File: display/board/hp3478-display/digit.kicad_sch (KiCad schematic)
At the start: 18 parts

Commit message: Reorganize schematic.
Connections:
- net A16: no longer D218.2 (A)
- net K: no longer D217.1 (K)
- new net: D217.1 (K), D218.2 (A)
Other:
- moved on the sheet: D201, D202, D203, D204, D205, D206, D207, D208, D209, D210, D211, D212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

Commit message: Add digit outlines and place LEDs.
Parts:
- D201, D202, D203, D204, D205, D206, D207, D208, D209, D210, D211, D212, D213, D214, D215, D216, D217, D218: footprint LED_SMD:LED_0402_1005Metric -> 0Local:LED_0402_1005Metric
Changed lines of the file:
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@@
       (effects (font (size 1.27 1.27)) (justify right))
     )
-    (property "Footprint" "LED_SMD:LED_0402_1005Metric" (id 2) (at 74.93 88.9 0)
+    (property "Footprint" "0Local:LED_0402_1005Metric" (id 2) (at 74.93 88.9 0)
       (effects (font (size 1.27 1.27)) hide)
     )
@@
       (effects (font (size 1.27 1.27)) (justify right))
     )
-    (property "Footprint" "LED_SMD:LED_0402_1005Metric" (id 2) (at 87.63 142.24 0)
+    (property "Footprint" "0Local:LED_0402_1005Metric" (id 2) (at 87.63 142.24 0)
       (effects (font (size 1.27 1.27)) hide)
     )
@@
       (effects (font (size 1.27 1.27)) (justify right))
     )
-    (property "Footprint" "LED_SMD:LED_0402_1005Metric" (id 2) (at 74.93 68.58 0)
+    (property "Footprint" "0Local:LED_0402_1005Metric" (id 2) (at 74.93 68.58 0)
       (effects (font (size 1.27 1.27)) hide)
     )
@@
       (effects (font (size 1.27 1.27)) (justify right))
     )
-    (property "Footprint" "LED_SMD:LED_0402_1005Metric" (id 2) (at 74.93 93.98 0)
+    (property "Footprint" "0Local:LED_0402_1005Metric" (id 2) (at 74.93 93.98 0)
       (effects (font (size 1.27 1.27)) hide)
     )
@@
       (effects (font (size 1.27 1.27)) (justify right))
     )
-    (property "Footprint" "LED_SMD:LED_0402_1005Metric" (id 2) (at 74.93 104.14 0)
+    (property "Footprint" "0Local:LED_0402_1005Metric" (id 2) (at 74.93 104.14 0)
       (effects (font (size 1.27 1.27)) hide)
     )
@@
       (effects (font (size 1.27 1.27)) (justify right))
     )
-    (property "Footprint" "LED_SMD:LED_0402_1005Metric" (id 2) (at 74.93 73.66 0)
+    (property "Footprint" "0Local:LED_0402_1005Metric" (id 2) (at 74.93 73.66 0)
       (effects (font (size 1.27 1.27)) hide)
     )
@@
       (effects (font (size 1.27 1.27)) (justify right))
     )
-    (property "Footprint" "LED_SMD:LED_0402_1005Metric" (id 2) (at 74.93 119.38 0)
+    (property "Footprint" "0Local:LED_0402_1005Metric" (id 2) (at 74.93 119.38 0)
       (effects (font (size 1.27 1.27)) hide)
     )
@@
       (effects (font (size 1.27 1.27)) (justify right))
     )
-    (property "Footprint" "LED_SMD:LED_0402_1005Metric" (id 2) (at 74.93 124.46 0)
+    (property "Footprint" "0Local:LED_0402_1005Metric" (id 2) (at 74.93 124.46 0)
       (effects (font (size 1.27 1.27)) hide)
     )
@@
       (effects (font (size 1.27 1.27)) (justify right))
     )
-    (property "Footprint" "LED_SMD:LED_0402_1005Metric" (id 2) (at 74.93 114.3 0)
+    (property "Footprint" "0Local:LED_0402_1005Metric" (id 2) (at 74.93 114.3 0)
       (effects (font (size 1.27 1.27)) hide)
     )
@@
       (effects (font (size 1.27 1.27)) (justify right))
     )
-    (property "Footprint" "LED_SMD:LED_0402_1005Metric" (id 2) (at 74.93 58.42 0)
+    (property "Footprint" "0Local:LED_0402_1005Metric" (id 2) (at 74.93 58.42 0)
       (effects (font (size 1.27 1.27)) hide)
     )
@@
       (effects (font (size 1.27 1.27)) (justify right))
     )
-    (property "Footprint" "LED_SMD:LED_0402_1005Metric" (id 2) (at 74.93 83.82 0)
+    (property "Footprint" "0Local:LED_0402_1005Metric" (id 2) (at 74.93 83.82 0)
       (effects (font (size 1.27 1.27)) hide)
     )
@@
       (effects (font (size 1.27 1.27)) (justify right))
     )
-    (property "Footprint" "LED_SMD:LED_0402_1005Metric" (id 2) (at 74.93 109.22 0)
+    (property "Footprint" "0Local:LED_0402_1005Metric" (id 2) (at 74.93 109.22 0)
       (effects (font (size 1.27 1.27)) hide)
     )
@@
       (effects (font (size 1.27 1.27)) (justify right))
     )
-    (property "Footprint" "LED_SMD:LED_0402_1005Metric" (id 2) (at 74.93 78.74 0)
+    (property "Footprint" "0Local:LED_0402_1005Metric" (id 2) (at 74.93 78.74 0)
       (effects (font (size 1.27 1.27)) hide)
     )
@@
       (effects (font (size 1.27 1.27)) (justify right))
     )
-    (property "Footprint" "LED_SMD:LED_0402_1005Metric" (id 2) (at 67.31 142.24 0)
+    (property "Footprint" "0Local:LED_0402_1005Metric" (id 2) (at 67.31 142.24 0)
       (effects (font (size 1.27 1.27)) hide)
     )
@@
       (effects (font (size 1.27 1.27)) (justify right))
     )
-    (property "Footprint" "LED_SMD:LED_0402_1005Metric" (id 2) (at 74.93 99.06 0)
+    (property "Footprint" "0Local:LED_0402_1005Metric" (id 2) (at 74.93 99.06 0)
       (effects (font (size 1.27 1.27)) hide)
     )
@@
       (effects (font (size 1.27 1.27)) (justify right))
     )
-    (property "Footprint" "LED_SMD:LED_0402_1005Metric" (id 2) (at 74.93 129.54 0)
+    (property "Footprint" "0Local:LED_0402_1005Metric" (id 2) (at 74.93 129.54 0)
       (effects (font (size 1.27 1.27)) hide)
     )
@@
       (effects (font (size 1.27 1.27)) (justify right))
     )
-    (property "Footprint" "LED_SMD:LED_0402_1005Metric" (id 2) (at 74.93 134.62 0)
+    (property "Footprint" "0Local:LED_0402_1005Metric" (id 2) (at 74.93 134.62 0)
       (effects (font (size 1.27 1.27)) hide)
     )
@@
       (effects (font (size 1.27 1.27)) (justify right))
     )
-    (property "Footprint" "LED_SMD:LED_0402_1005Metric" (id 2) (at 74.93 63.5 0)
-      (effects (font (size 1.27 1.27)) hide)
-    )
+    (property "Footprint" "0Local:LED_0402_1005Metric" (id 2) (at 74.93 63.5 0)
+      (effects (font (size 1.27 1.27)) hide)
+    )

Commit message: Remove MCU and move annunciator LEDs to their own matrix row.
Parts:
- removed D217, D218: LED, 0Local:LED_0402_1005Metric, symbol Device:LED
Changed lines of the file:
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@@
   (junction (at 101.6 124.46) (diameter 0) (color 0 0 0 0)
   )
-  (junction (at 101.6 142.24) (diameter 0) (color 0 0 0 0)
-  )
   (junction (at 101.6 88.9) (diameter 0) (color 0 0 0 0)
   )
@@
     (stroke (width 0) (type default) (color 0 0 0 0))
   )
-  (bus_entry (at 50.8 139.7) (size 2.54 2.54)
-    (stroke (width 0) (type default) (color 0 0 0 0))
-  )
   (bus_entry (at 50.8 81.28) (size 2.54 2.54)
     (stroke (width 0) (type default) (color 0 0 0 0))
@@
     (stroke (width 0) (type default) (color 0 0 0 0))
   )
-  (wire (pts (xy 53.34 142.24) (xy 63.5 142.24))
-    (stroke (width 0) (type default) (color 0 0 0 0))
-  )
   (wire (pts (xy 53.34 129.54) (xy 71.12 129.54))
     (stroke (width 0) (type default) (color 0 0 0 0))
@@
     (stroke (width 0) (type default) (color 0 0 0 0))
   )
-  (bus (pts (xy 50.8 139.7) (xy 50.8 132.08))
-    (stroke (width 0) (type default) (color 0 0 0 0))
-  )
   (bus (pts (xy 50.8 76.2) (xy 50.8 71.12))
     (stroke (width 0) (type default) (color 0 0 0 0))
@@
     (stroke (width 0) (type default) (color 0 0 0 0))
   )
-  (wire (pts (xy 91.44 157.48) (xy 101.6 157.48))
+  (wire (pts (xy 91.44 144.78) (xy 101.6 144.78))
     (stroke (width 0) (type default) (color 0 0 0 0))
   )
@@
     (stroke (width 0) (type default) (color 0 0 0 0))
   )
-  (wire (pts (xy 101.6 142.24) (xy 101.6 157.48))
-    (stroke (width 0) (type default) (color 0 0 0 0))
-  )
   (wire (pts (xy 78.74 119.38) (xy 101.6 119.38))
     (stroke (width 0) (type default) (color 0 0 0 0))
@@
     (stroke (width 0) (type default) (color 0 0 0 0))
   )
-  (wire (pts (xy 91.44 142.24) (xy 101.6 142.24))
-    (stroke (width 0) (type default) (color 0 0 0 0))
-  )
   (bus (pts (xy 50.8 96.52) (xy 50.8 91.44))
     (stroke (width 0) (type default) (color 0 0 0 0))
@@
     (stroke (width 0) (type default) (color 0 0 0 0))
   )
-  (wire (pts (xy 101.6 134.62) (xy 101.6 142.24))
+  (wire (pts (xy 101.6 134.62) (xy 101.6 144.78))
     (stroke (width 0) (type default) (color 0 0 0 0))
   )
@@
     (stroke (width 0) (type default) (color 0 0 0 0))
   )
-  (wire (pts (xy 71.12 142.24) (xy 83.82 142.24))
-    (stroke (width 0) (type default) (color 0 0 0 0))
-  )
   (wire (pts (xy 101.6 83.82) (xy 101.6 88.9))
     (stroke (width 0) (type default) (color 0 0 0 0))
@@
     (effects (font (size 1.27 1.27)) (justify left bottom))
   )
-  (label "A16" (at 55.88 142.24 0)
-    (effects (font (size 1.27 1.27)) (justify left bottom))
-  )
   (label "A11" (at 55.88 114.3 0)
     (effects (font (size 1.27 1.27)) (justify left bottom))
@@
     (effects (font (size 1.27 1.27)) (justify left bottom))
   )
-  (hierarchical_label "A[0..16]" (shape input) (at 40.64 50.8 180)
+  (hierarchical_label "A[0..15]" (shape input) (at 40.64 50.8 180)
     (effects (font (size 1.27 1.27)) (justify right))
   )
-  (hierarchical_label "K" (shape input) (at 91.44 157.48 180)
+  (hierarchical_label "K" (shape input) (at 91.44 144.78 180)
     (effects (font (size 1.27 1.27)) (justify right))
   )
@@
     )
     (property "Datasheet" "~" (id 3) (at 74.93 88.9 0)
-      (effects (font (size 1.27 1.27)) hide)
-    )
-    (pin "1")
-    (pin "2")
-  )
-  (symbol (lib_id "Device:LED") (at 87.63 142.24 180) (unit 1)
-    (in_bom yes) (on_board yes)
-    (property "Reference" "D218" (id 0) (at 85.09 143.51 0)
-      (effects (font (size 1.27 1.27)) (justify left))
-    )
-    (property "Value" "LED" (id 1) (at 90.17 143.51 0)
-      (effects (font (size 1.27 1.27)) (justify right))
-    )
-    (property "Footprint" "0Local:LED_0402_1005Metric" (id 2) (at 87.63 142.24 0)
-      (effects (font (size 1.27 1.27)) hide)
-    )
-    (property "Datasheet" "~" (id 3) (at 87.63 142.24 0)
       (effects (font (size 1.27 1.27)) hide)
     )
@@
       (effects (font (size 1.27 1.27)) hide)
     )
-    (pin "1")
-    (pin "2")
-  )
-  (symbol (lib_id "Device:LED") (at 67.31 142.24 180) (unit 1)
-    (in_bom yes) (on_board yes)
-    (property "Reference" "D217" (id 0) (at 64.77 143.51 0)
-      (effects (font (size 1.27 1.27)) (justify left))
-    )
-    (property "Value" "LED" (id 1) (at 69.85 143.51 0)
-      (effects (font (size 1.27 1.27)) (justify right))
-    )
-    (property "Footprint" "0Local:LED_0402_1005Metric" (id 2) (at 67.31 142.24 0)
-      (effects (font (size 1.27 1.27)) hide)
-    )
-    (property "Datasheet" "~" (id 3) (at 67.31 142.24 0)
-      (effects (font (size 1.27 1.27)) hide)
-    )

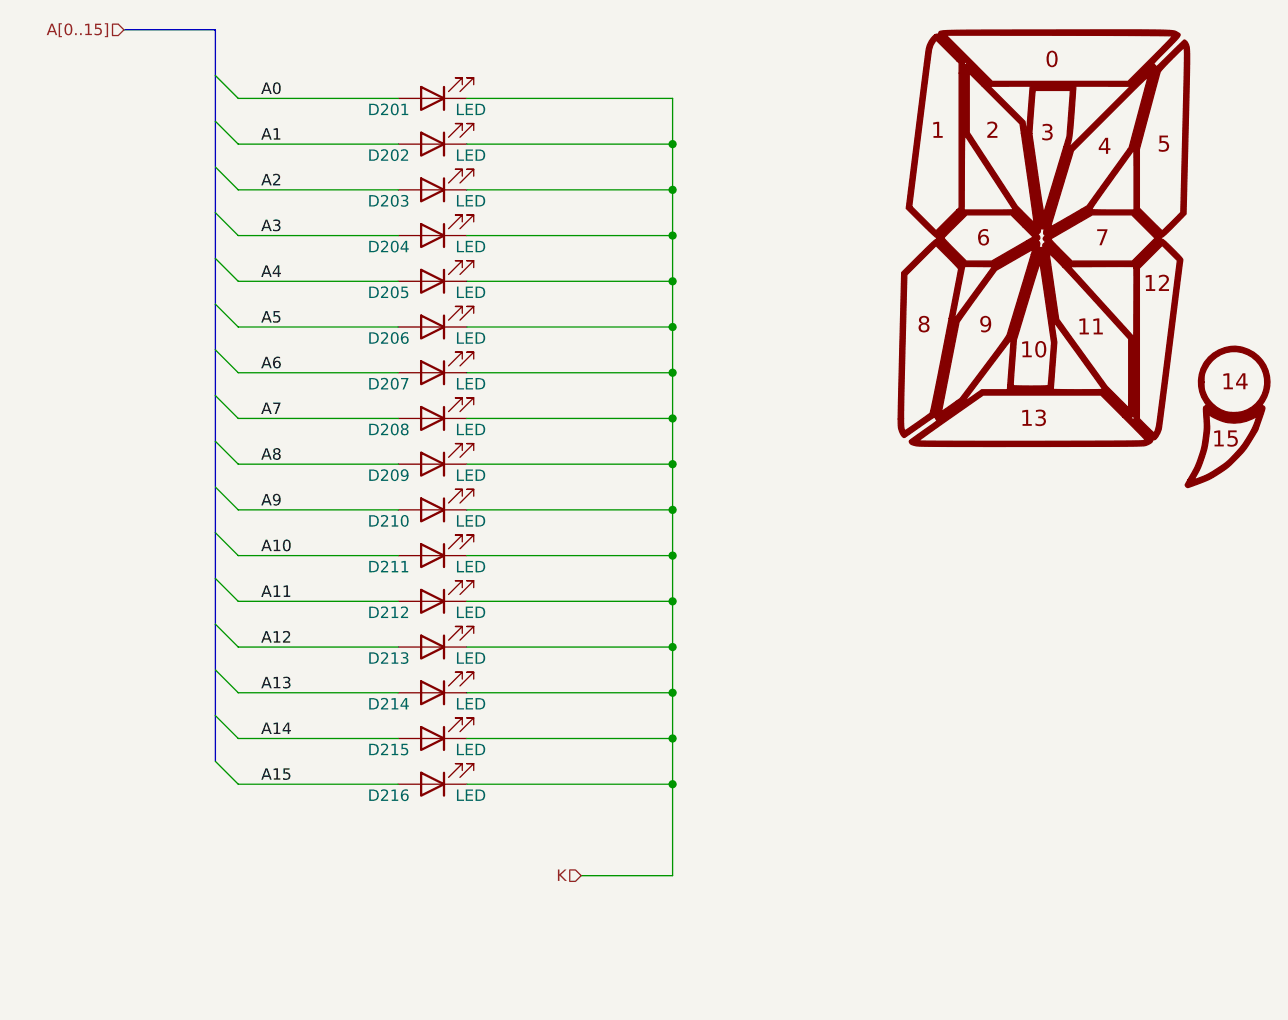
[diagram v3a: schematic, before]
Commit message: Add missing colon segment and adjust scan matrix.
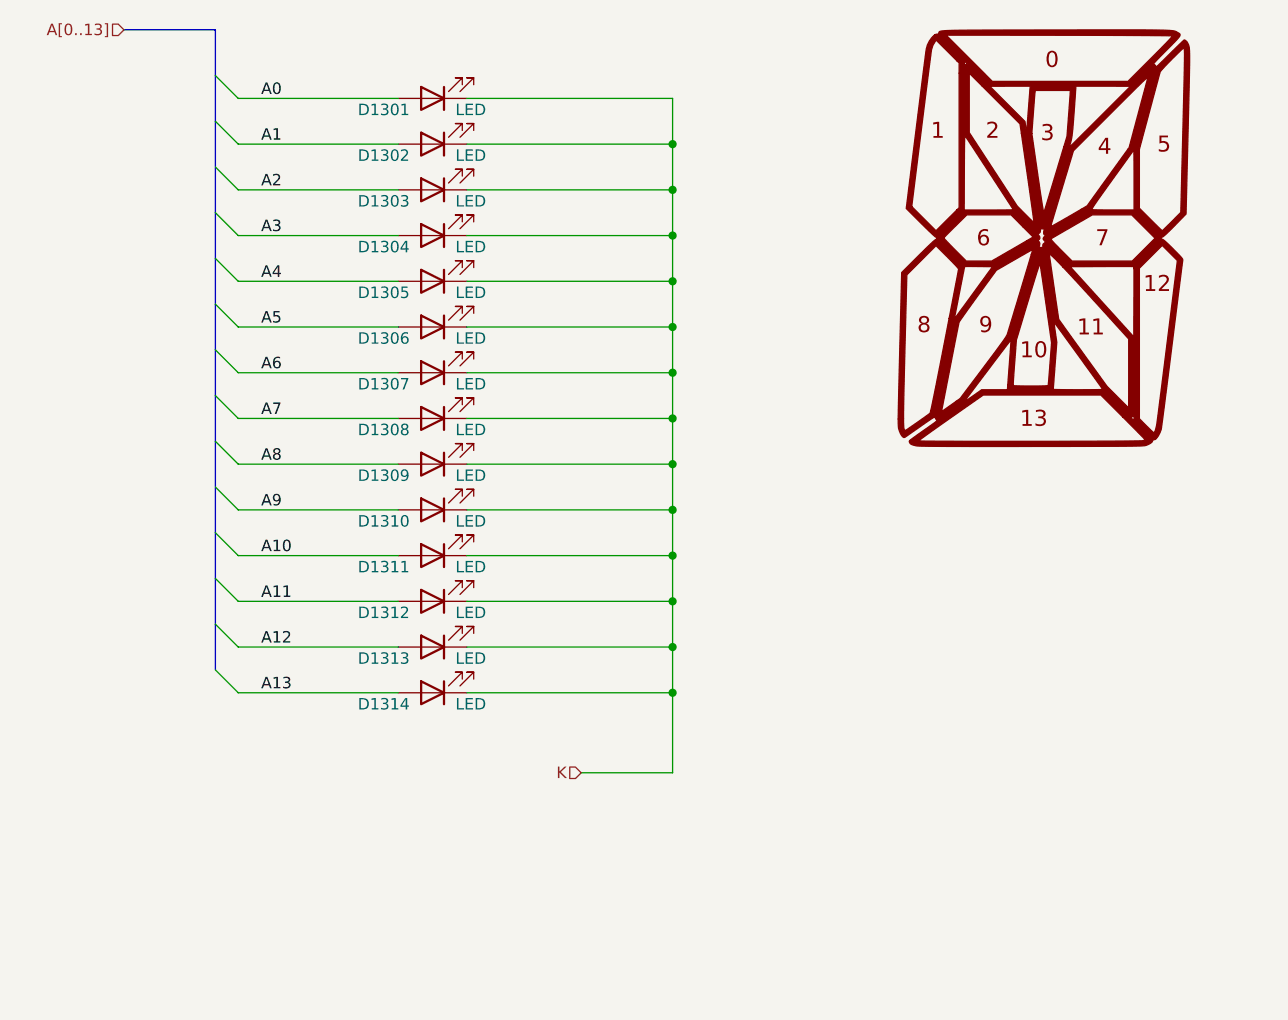
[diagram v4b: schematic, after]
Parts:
- removed D215, D216: LED, 0Local:LED_0402_1005Metric, symbol Device:LED
- renumbered D201 to D1301, D202 to D1302, D203 to D1303, D204 to D1304, D205 to D1305, D206 to D1306, D207 to D1307, D208 to D1308, D209 to D1309, D210 to D1310, D211 to D1311, D212 to D1312, D213 to D1313, D214 to D1314
